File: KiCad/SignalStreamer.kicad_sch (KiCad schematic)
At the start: 28 parts, among them J101 Conn_01x01, J102 Conn_01x01, J103 Conn_01x01, J104 Conn_01x01, J105 Conn_01x02, T101 Coupled_Inductors_2

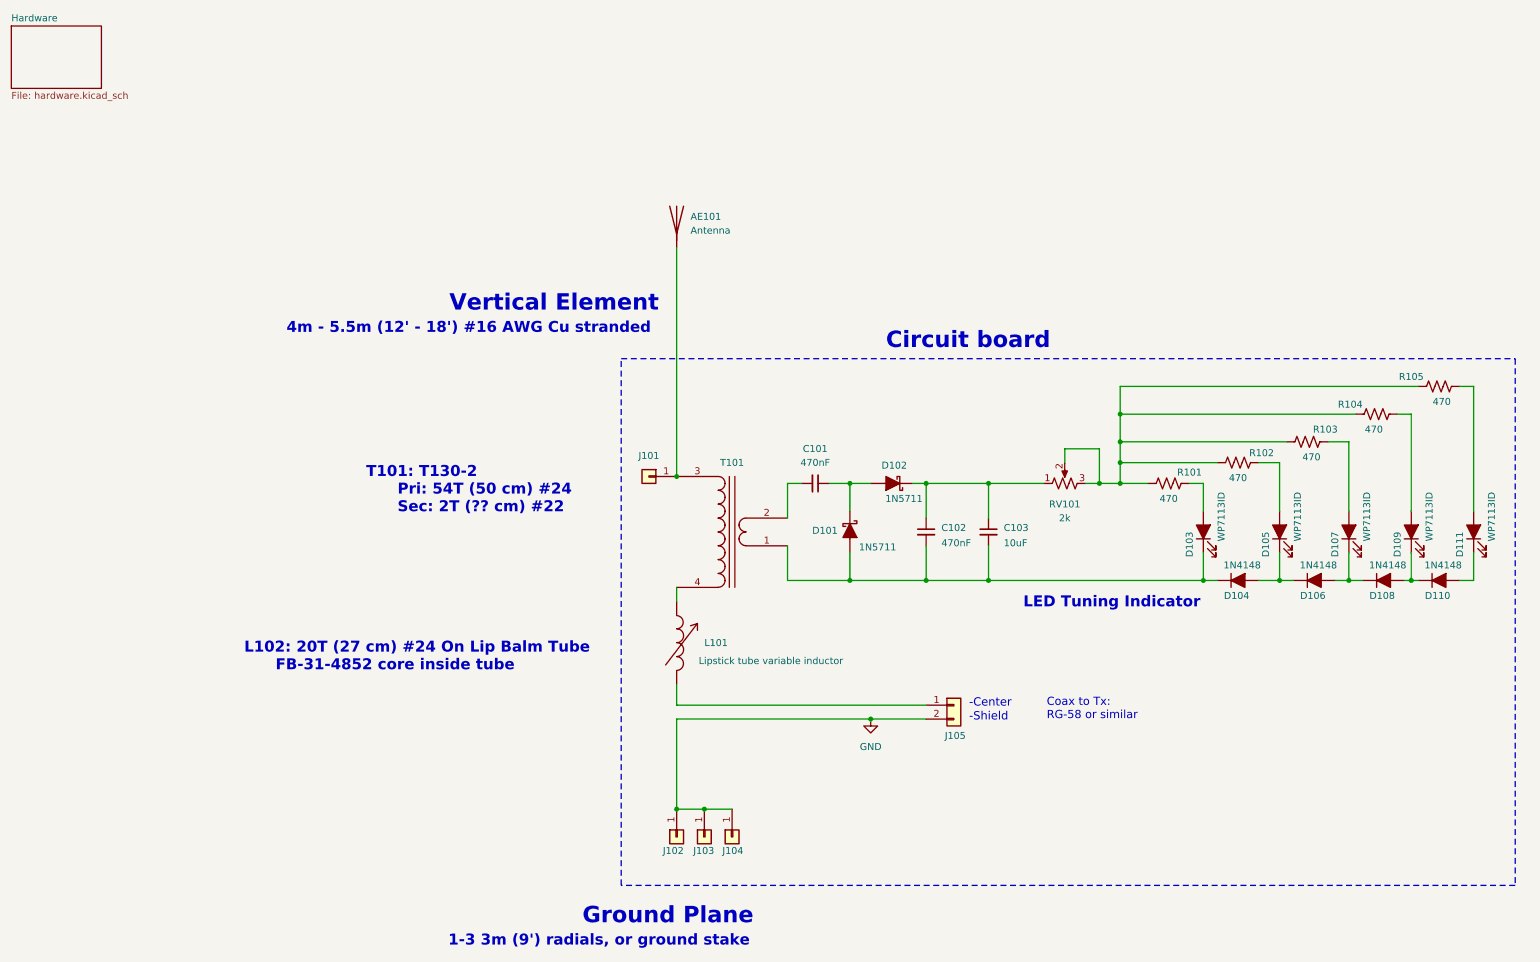
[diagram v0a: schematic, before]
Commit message: Updates
Added bypass capacitors across diodes
10k pot, now wired as potentiometer
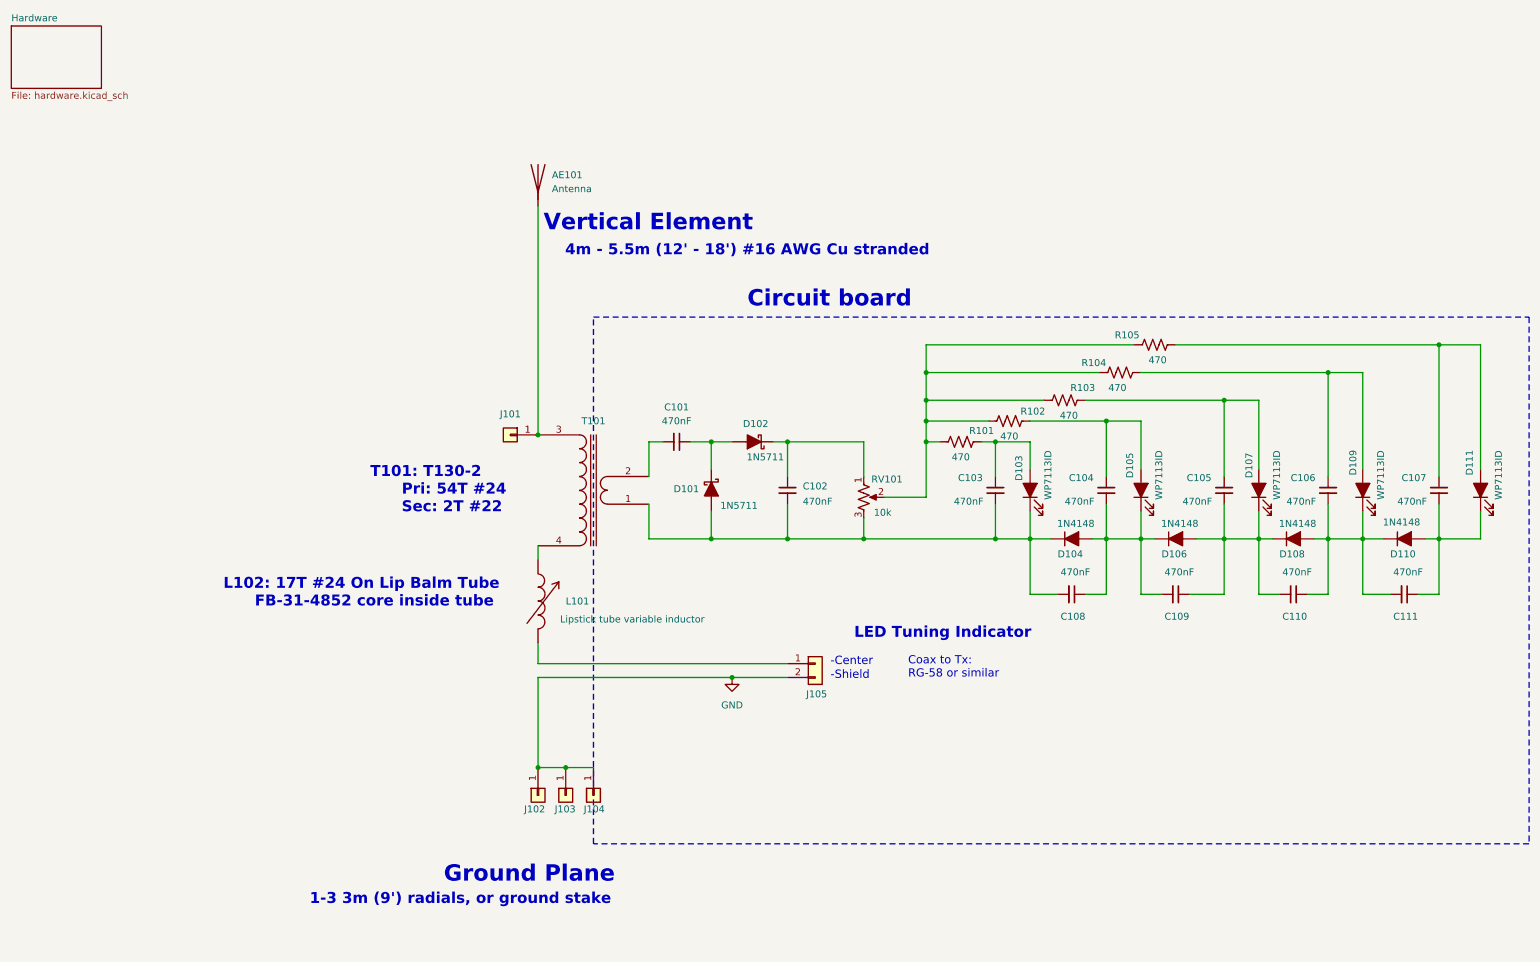
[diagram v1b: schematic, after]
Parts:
- added C104, C105, C106, C107, C108, C109, C110, C111: 470nF, Capacitor_THT:C_Disc_D3.0mm_W2.0mm_P2.50mm, symbol Device:C_Small
- C103: value 10uF -> 470nF; footprint Capacitor_THT:CP_Radial_Tantal_D5.5mm_P2.50mm -> Capacitor_THT:C_Disc_D3.0mm_W2.0mm_P2.50mm; Digi-Key Part No. 478-1839-ND -> 445-180414-1-ND; Link https://www.digikey.com/en/products/detail/kyocera-avx/TAP1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 -> https://www.digikey.com/en/products/detail/tdk-corporation/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; Manufacturer KYOCERA AVX -> TDK Corporation; Manufacturer PN TAP106K016SCS -> FA14X7S2A474KRU06
- RV101: value 2k -> 10k
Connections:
- net at D104.2 (A), D105.1 (K), D106.1 (K): now also C104.2, C108.1, C109.2
- net at D106.2 (A), D107.1 (K), D108.1 (K): now also C105.2, C109.1, C110.2
- net at R101.1, R102.1, R103.1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: no longer RV101.3
- net at D105.2 (A), R102.2: now also C104.1
- net at C102.2, C103.2, D101.2 (A)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: now also RV101.3, C108.2
- net at D103.2 (A), R101.2: now also C103.1
- net at D107.2 (A), R103.2: now also C105.1
- net at C102.1, D102.1 (K), RV101.1: no longer C103.1
- net at D111.2 (A), R105.2: now also C107.1
- net at D109.2 (A), R104.2: now also C106.1
- net at D110.2 (A), D111.1 (K): now also C107.2, C111.1
- net at D108.2 (A), D109.1 (K), D110.1 (K): now also C106.2, C110.1, C111.2
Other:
- note added: "L102: 17T #24 On Lip Balm Tube FB-31-4852 core inside tube"
- note added: "T101: T130-2 Pri: 54T #24 Sec: 2T #22"
- note removed: "L102: 20T (27 cm) #24 On Lip Balm Tube FB-31-4852 core inside tube"
- note removed: "T101: T130-2 Pri: 54T (50 cm) #24 Sec: 2T (?? cm) #22"
- title: 80m Bottom-Loaded Vertical Fox Antenna -> 80m Base-Loaded Vertical Fox Antenna
- moved on the sheet: AE101, C101, C102, D101, D102, D103, D104, D105, D106, D107, D108, D109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

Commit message: Update SignalStreamer.kicad_sch
Moving to SMD components
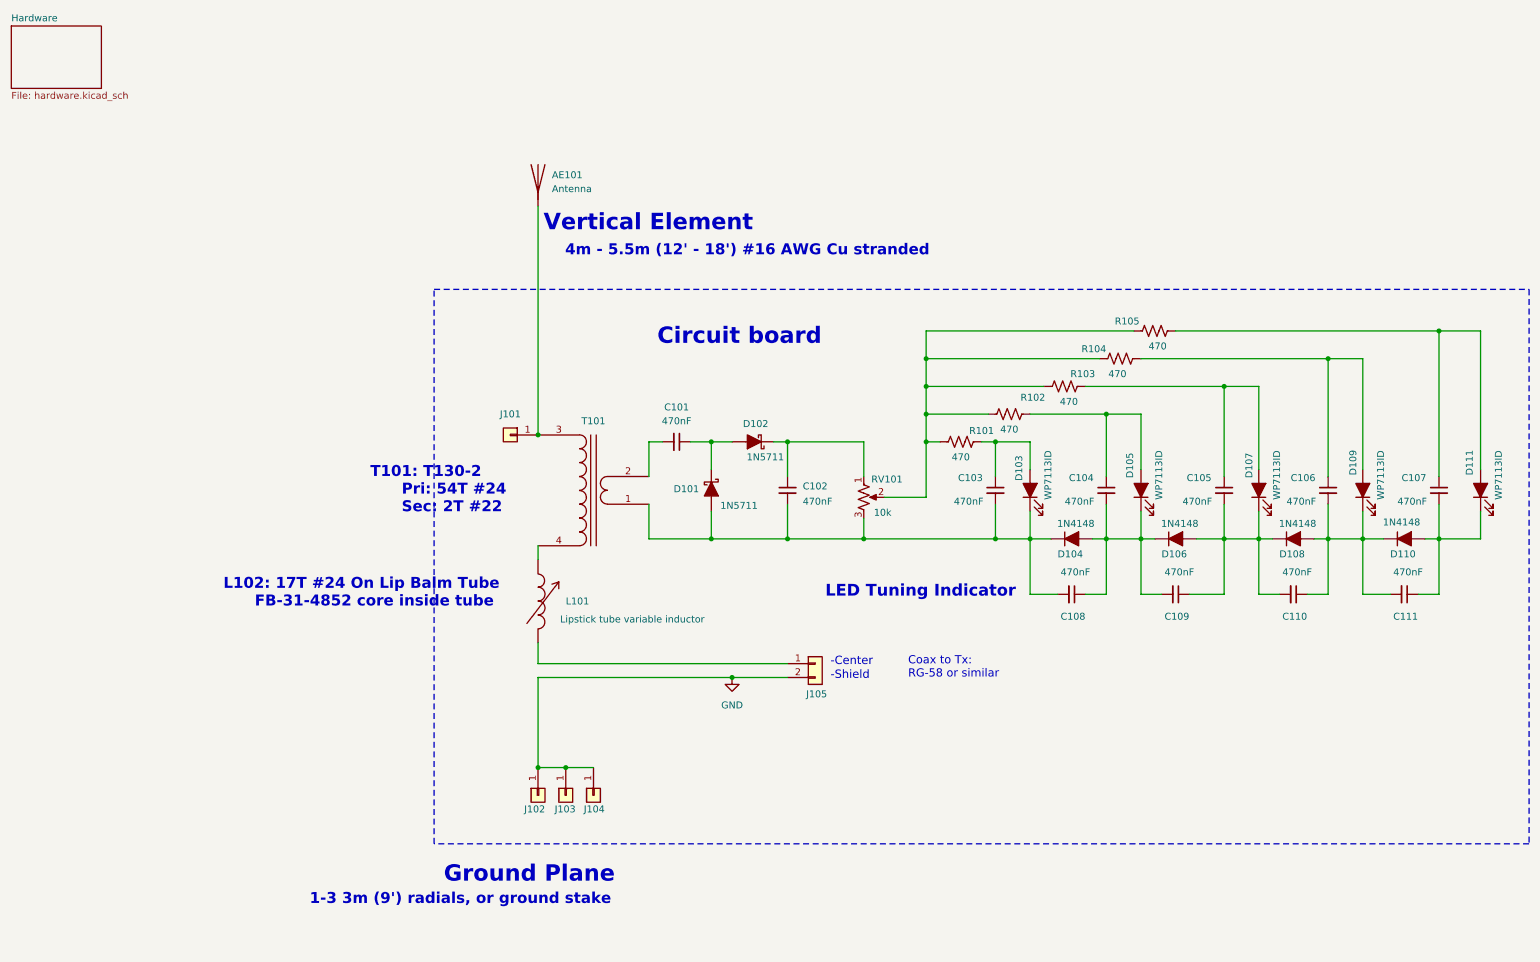
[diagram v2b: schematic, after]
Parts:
- C101, C102, C103, C104, C105, C106, C107, C108, C109, C110, C111: footprint Capacitor_THT:C_Disc_D3.0mm_W2.0mm_P2.50mm -> Capacitor_SMD:C_0805_2012Metric
- R101, R102, R103, R104, R105: footprint Resistor_THT:R_Axial_DIN0207_L6.3mm_D2.5mm_P5.08mm_Vertical -> Resistor_SMD:R_0805_2012Metric
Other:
- moved on the sheet: R102, R103, R104, R105

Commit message: Design Updates
Changes to improve LED illumination for better tuning indication. This will become SignalStreamer Ver 1.1. The PCB design has not yet been updated.
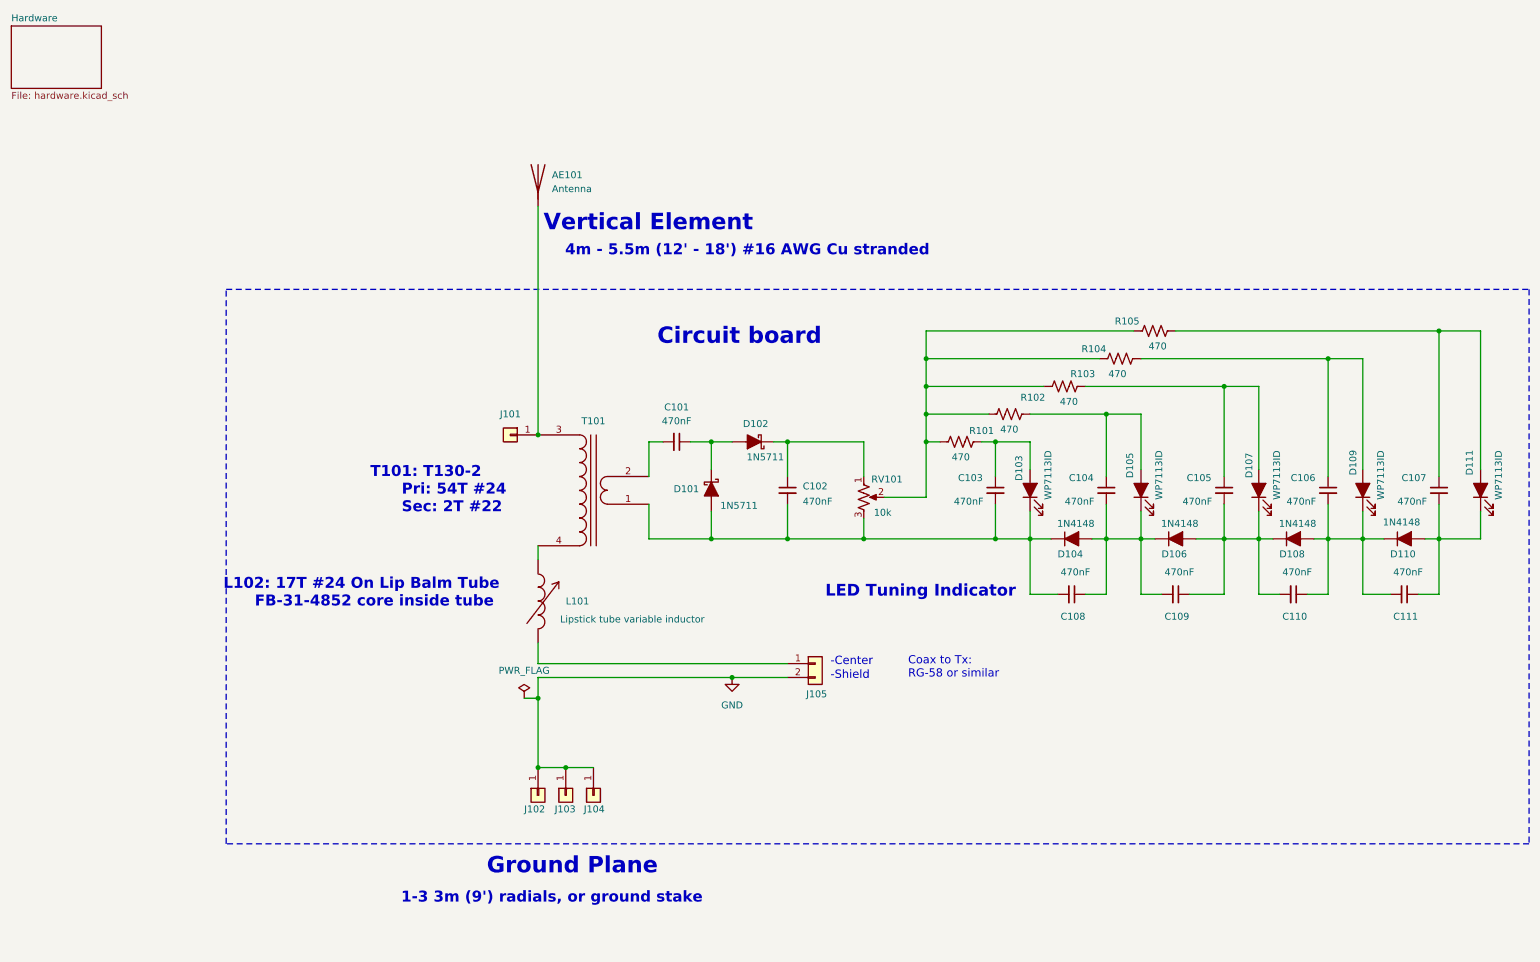
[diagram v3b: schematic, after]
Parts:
- C101, C102, C103, C104, C105, C106, C107, C108, C109, C110, C111: Digi-Key Part No. 445-180414-1-ND -> 478-KGM21AR71H474JUCT-ND; Link https://www.digikey.com/en/products/detail/tdk-corporation/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 -> https://www.digikey.com/en/products/detail/kyocera-avx/KGM2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; Manufacturer TDK Corporation -> KYOCERA AVX; Manufacturer PN FA14X7S2A474KRU06 -> KGM21AR71H474JU
- D101, D102: footprint Diode_THT:D_DO-35_SOD27_P7.62mm_Horizontal -> Diode_SMD:D_SOD-123; Digi-Key Part No. 497-2499-1-ND -> 1N5711W-FDICT-ND; Link https://www.digikey.com/en/products/detail/stmicroelectroni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 -> https://www.digikey.com/en/products/detail/diodes-incorpora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; Manufacturer STMicroelectronics -> Diodes Incorporated; Manufacturer PN 1N5711 -> 1N5711W-7-F
- D104, D106, D108, D110: footprint Diode_THT:D_DO-35_SOD27_P2.54mm_Vertical_KathodeUp -> Diode_SMD:D_SOD-123; Digi-Key Part No. 1N4148FS-ND -> 1N4148W-FDICT-ND; Link https://www.digikey.com/en/products/detail/onsemi/1N4148/45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 -> https://www.digikey.com/en/products/detail/diodes-incorpora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; Manufacturer onsemi -> Diodes Incorporated; Manufacturer PN 1N4148 -> 1N4148W-7-F
- R101, R102, R103, R104, R105: Digi-Key Part No. CF18JT470RCT-ND -> 311-470CRCT-ND; Link https://www.digikey.com/en/products/detail/stackpole-electr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 -> https://www.digikey.com/en/products/detail/yageo/RC0805FR-0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; Manufacturer Stackpole Electronics Inc -> YAGEO; Manufacturer PN CF18JT470R -> RC0805FR-07470RL
